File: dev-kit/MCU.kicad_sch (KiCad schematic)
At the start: 38 parts, among them IC301 FAN5622SX, IC302 MX25U51245GZ4I00, IC303 USBLC6-2P6, IC304 NTS0104GU12, J301 Jumper, J302 Jumper, J303 Jumper, J304 Jumper, M301 NORA-B106, X301 Power, X302 Power, X303 Device, X304 GPIO, X305 UART, X306 IO Power, X307 Display, X308 Touch Power, X309 LED Power, X310 DEBUG

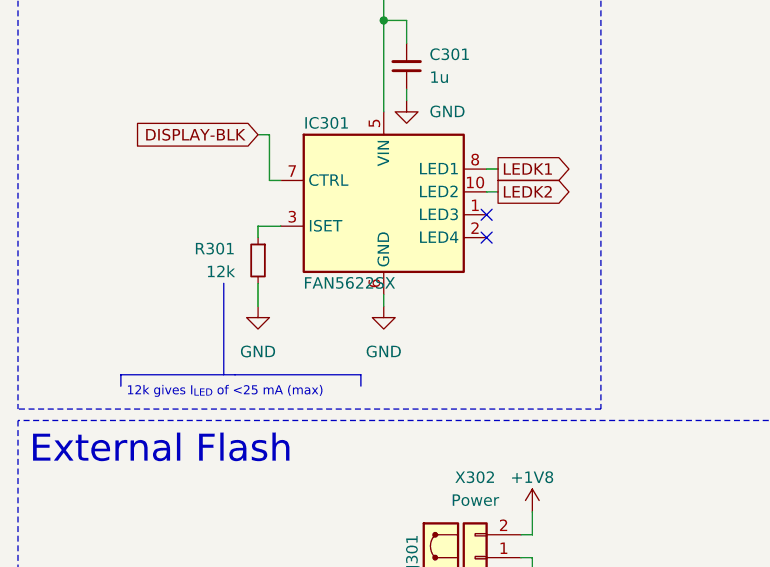
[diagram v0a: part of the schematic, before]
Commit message: Fix wrong part numbers
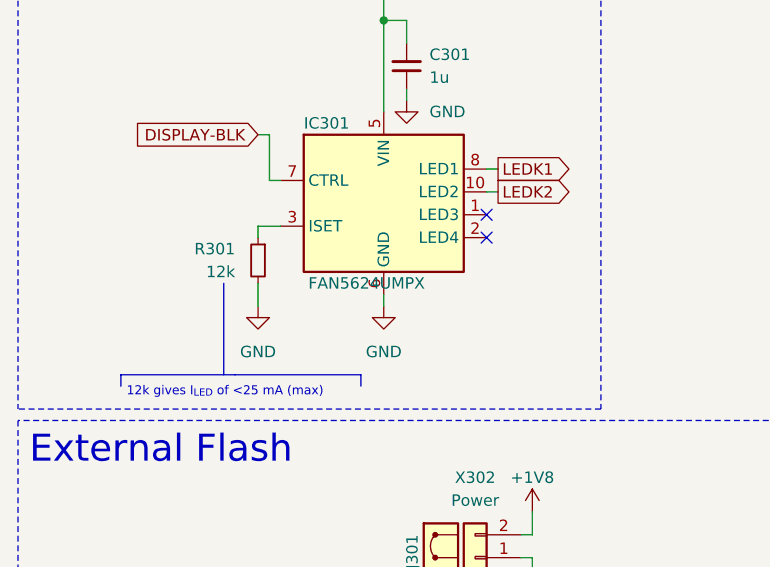
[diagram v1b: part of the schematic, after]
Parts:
- IC301: value FAN5622SX -> FAN5624UMPX
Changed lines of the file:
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@@
 			)
 		)
-		(property "Value" "FAN5622SX"
-			(at 49.53 204.47 0)
+		(property "Value" "FAN5624UMPX"
+			(at 51.435 204.47 0)
 			(effects
 				(font
